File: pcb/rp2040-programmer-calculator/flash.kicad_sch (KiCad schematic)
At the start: 5 parts, among them SW63 PTS526SM20SMTR21 LFS, U7 W25Q32JVSS

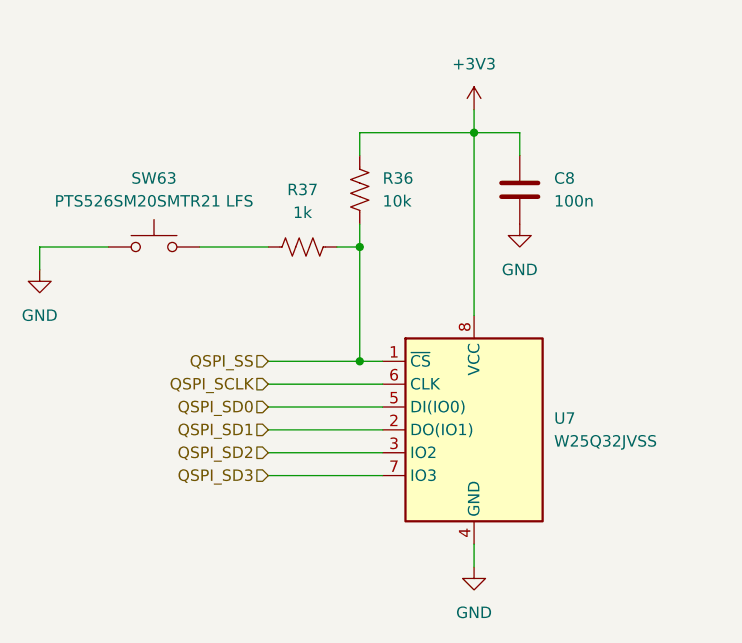
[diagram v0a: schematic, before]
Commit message: Finish schematic
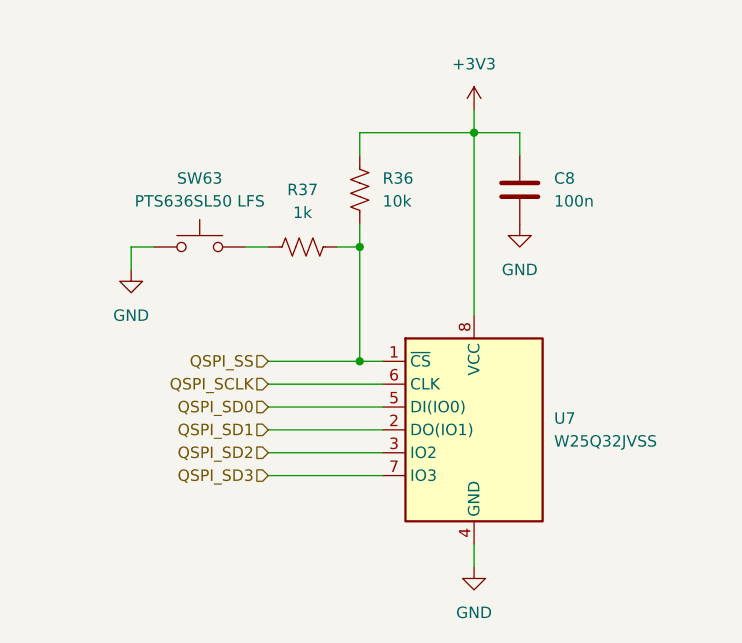
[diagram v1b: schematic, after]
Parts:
- SW63: value PTS526SM20SMTR21 LFS -> PTS636SL50 LFS; footprint Button_Switch_SMD:SW_Push_1P1T_XKB_TS-1187A -> SamacSys_Parts:PTS636SL50LFS

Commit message: Finish PCB
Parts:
- C8: footprint Capacitor_SMD:C_0402_1005Metric -> Capacitor_SMD:C_0603_1608Metric
- R40: renamed from R36; footprint (none) -> Resistor_SMD:R_0603_1608Metric
- R41: renamed from R37; footprint (none) -> Resistor_SMD:R_0603_1608Metric
- renumbered SW63 to SW64
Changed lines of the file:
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@@
 		(dnp no)
 		(fields_autoplaced yes)
-		(property "Reference" "R37"
+		(property "Reference" "R41"
 			(at 130.81 86.36 90)
 			(effects
@@
 			)
 		)
-		(property "Footprint" ""
+		(property "Footprint" "Resistor_SMD:R_0603_1608Metric"
 			(at 131.064 91.694 90)
 			(effects
@@
 			(project ""
 				(path "/a76e07d4-0b9a-412a-8673-6db50899653e/8d49ad97-c789-456a-9694-57f2a89048ae"
-					(reference "R37")
+					(reference "R41")
 					(unit 1)
 				)
@@
 		(dnp no)
 		(fields_autoplaced yes)
-		(property "Reference" "#PWR027"
+		(property "Reference" "#PWR034"
 			(at 154.94 96.52 0)
 			(effects
@@
 			(project "rp2040-programmer-calculator"
 				(path "/a76e07d4-0b9a-412a-8673-6db50899653e/8d49ad97-c789-456a-9694-57f2a89048ae"
-					(reference "#PWR027")
+					(reference "#PWR034")
 					(unit 1)
 				)
@@
 		(dnp no)
 		(fields_autoplaced yes)
-		(property "Reference" "R36"
+		(property "Reference" "R40"
 			(at 139.7 85.0899 0)
 			(effects
@@
 			)
 		)
-		(property "Footprint" ""
+		(property "Footprint" "Resistor_SMD:R_0603_1608Metric"
 			(at 138.176 86.614 90)
 			(effects
@@
 			(project ""
 				(path "/a76e07d4-0b9a-412a-8673-6db50899653e/8d49ad97-c789-456a-9694-57f2a89048ae"
-					(reference "R36")
+					(reference "R40")
 					(unit 1)
 				)
@@
 		(dnp no)
 		(fields_autoplaced yes)
-		(property "Reference" "#PWR026"
+		(property "Reference" "#PWR033"
 			(at 149.86 81.28 0)
 			(effects
@@
 			(project "rp2040-programmer-calculator"
 				(path "/a76e07d4-0b9a-412a-8673-6db50899653e/8d49ad97-c789-456a-9694-57f2a89048ae"
-					(reference "#PWR026")
+					(reference "#PWR033")
 					(unit 1)
 				)
@@
 		(dnp no)
 		(fields_autoplaced yes)
-		(property "Reference" "SW63"
+		(property "Reference" "SW64"
 			(at 119.38 85.09 0)
 			(effects
@@
 			(project "rp2040-programmer-calculator"
 				(path "/a76e07d4-0b9a-412a-8673-6db50899653e/8d49ad97-c789-456a-9694-57f2a89048ae"
-					(reference "SW63")
+					(reference "SW64")
 					(unit 1)
 				)
@@
 			)
 		)
-		(property "Footprint" "Capacitor_SMD:C_0402_1005Metric"
+		(property "Footprint" "Capacitor_SMD:C_0603_1608Metric"
 			(at 155.9052 90.17 0)
 			(effects
@@
 		(dnp no)
 		(fields_autoplaced yes)
-		(property "Reference" "#PWR028"
+		(property "Reference" "#PWR035"
 			(at 111.76 101.6 0)
 			(effects
@@
 			(project "rp2040-programmer-calculator"
 				(path "/a76e07d4-0b9a-412a-8673-6db50899653e/8d49ad97-c789-456a-9694-57f2a89048ae"
-					(reference "#PWR028")
+					(reference "#PWR035")
 					(unit 1)
 				)
@@
 		(dnp no)
 		(fields_autoplaced yes)
-		(property "Reference" "#PWR029"
+		(property "Reference" "#PWR036"
 			(at 149.86 134.62 0)
 			(effects
@@
 			(project "rp2040-programmer-calculator"
 				(path "/a76e07d4-0b9a-412a-8673-6db50899653e/8d49ad97-c789-456a-9694-57f2a89048ae"
-					(reference "#PWR029")
-					(unit 1)
-				)
+					(reference "#PWR036")
+					(unit 1)
+				)

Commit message: Finished design
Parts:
- removed SW64: PTS636SL50 LFS, SamacSys_Parts:PTS636SL50LFS, symbol Switch:SW_Push
- removed U7: W25Q32JVSS, Package_SO:SOIC-8_5.23x5.23mm_P1.27mm, symbol Memory_Flash:W25Q32JVSS
- added SW66: PTS815_SJM_250_SMTR_LFS, PTS815_SJM_250_SMTR_LFS:SW_Push_PTS815_SJM_250_SMTR_LFS, symbol Switch:SW_Push
- added U7: W25Q16JVSS, Package_SO:SOIC-8_5.3x5.3mm_P1.27mm, symbol Memory_Flash:W25Q16JVSS
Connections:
- net +3V3: now also U7.8 (VCC)
- net GND: now also SW66.1, U7.4 (GND)
- net QSPI_SCLK: now also U7.6 (CLK)
- net QSPI_SD0: now also U7.5 (DI/IO_{0})
- net QSPI_SD1: now also U7.2 (DO/IO_{1})
- net QSPI_SD2: now also U7.3 (~{WP}/IO_{2})
- net QSPI_SD3: now also U7.7 (~{HOLD}/~{RESET}/IO_{3})
- net QSPI_SS: now also U7.1 (~{CS})
- net at R41.1: now also SW66.2
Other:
- moved on the sheet: C8, R40, R41
